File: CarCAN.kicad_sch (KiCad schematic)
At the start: 17 parts, among them IC1 TCAN337DCNR, J11 CarCANConnector, J2 CarCANConnector, U13 CDSOT23-T24CAN, U14 MCP2515-E/STVAO, Y4 8 MHz

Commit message: changed usb to be simpler (no inbuilt hub)
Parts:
- IC1: Arrow Part Number TCAN337DCNR -> (none); Arrow Price/Stock https://www.arrow.com/en/products/tcan337dcnr/texas-instrum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 -> (none); Height 1.45 -> (none); Manufacturer_Name Texas Instruments -> (none); Manufacturer_Part_Number TCAN337DCNR -> (none); Mouser Part Number 595-TCAN337DCNR -> (none); Mouser Price/Stock https://www.mouser.co.uk/ProductDetail/Texas-Instruments/TC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 -> (none)
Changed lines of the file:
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@@
-			)
-		)
-		(property "Height" "1.45"
-			(at 102.87 519.38 0)
-			(effects
-				(font
-					(size 1.27 1.27)
-				)
-				(justify left top)
-				(hide yes)
-			)
-		)
-		(property "Manufacturer_Name" "Texas Instruments"
-			(at 102.87 619.38 0)
-			(effects
-				(font
-					(size 1.27 1.27)
-				)
-				(justify left top)
-				(hide yes)
-			)
-		)
-		(property "Manufacturer_Part_Number" "TCAN337DCNR"
-			(at 102.87 719.38 0)
-			(effects
-				(font
-					(size 1.27 1.27)
-				)
-				(justify left top)
-				(hide yes)
-			)
-		)
-		(property "Mouser Part Number" "595-TCAN337DCNR"
-			(at 102.87 819.38 0)
-			(effects
-				(font
-					(size 1.27 1.27)
-				)
-				(justify left top)
-				(hide yes)
-			)
-		)
-		(property "Mouser Price/Stock" "https://www.mouser.co.uk/ProductDetail/Texas-Instruments/TCAN337DCNR?qs=gMfM3zrbS4r1ZrvbjcW09A%3D%3D"
-			(at 102.87 919.38 0)
-			(effects
-				(font
-					(size 1.27 1.27)
-				)
-				(justify left top)
-				(hide yes)
-			)
-		)
-		(property "Arrow Part Number" "TCAN337DCNR"
-			(at 102.87 1019.38 0)
-			(effects
-				(font
-					(size 1.27 1.27)
-				)
-				(justify left top)
-				(hide yes)
-			)
-		)
-		(property "Arrow Price/Stock" "https://www.arrow.com/en/products/tcan337dcnr/texas-instruments?region=nac"
-			(at 102.87 1119.38 0)
-			(effects
-				(font
-					(size 1.27 1.27)
-				)
-				(justify left top)
-				(hide yes)
 			)
 		)
@@
 			)
 		)
-		(property "Datasheet" "~"
+		(property "Datasheet" "https://abracon.com/Resonators/ABM3.pdf"
 			(at 99.06 58.42 0)
 			(effects
@@
 			)
 		)
-		(property "Datasheet" "~"
+		(property "Datasheet" "https://content.kemet.com/datasheets/KEM_C1002_X7R_SMD.pdf"
 			(at 55.88 137.16 0)
 			(effects

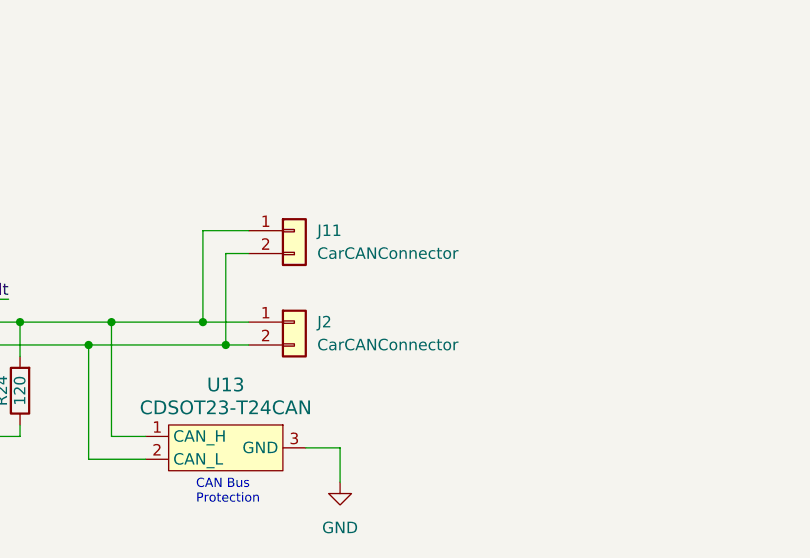
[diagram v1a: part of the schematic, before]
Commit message: moved everything to front & 0603'd stuff
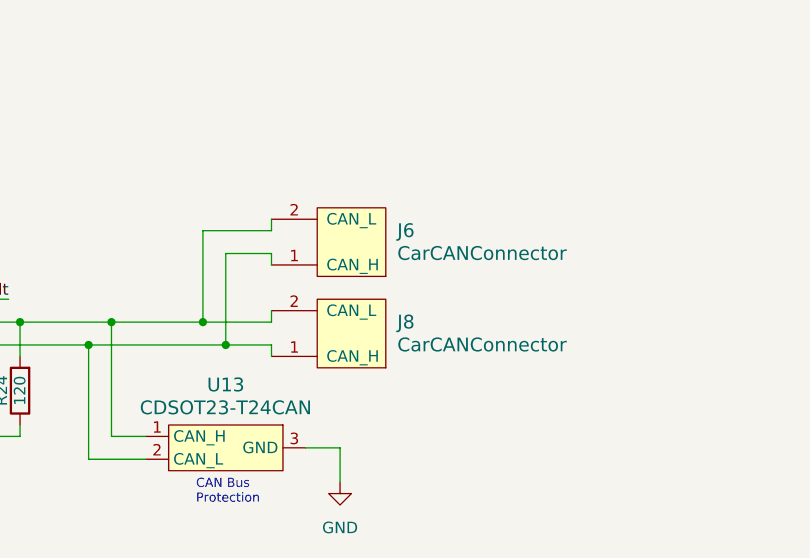
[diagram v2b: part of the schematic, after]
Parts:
- removed J11, J2: CarCANConnector, Connector_Molex:Molex_Micro-Fit_3.0_43650-0215_1x02_P3.00mm_Vertical, symbol Connector_Generic:Conn_01x02
- added J6, J8: CarCANConnector, UTSVT_Connectors:Molex_Nano-Fit_105309-xx02_1x02_P2.50mm_Vertical, symbol utsvt_connectors:CarCANConnector
- C11, C24, C25, C36, C37: footprint Capacitor_SMD:C_0805_2012Metric -> Capacitor_SMD:C_0603_1608Metric
- D4: footprint LED_SMD:LED_0805_2012Metric -> LED_SMD:LED_0603_1608Metric
- R2, R24, R34, R35: footprint Resistor_SMD:R_0805_2012Metric -> Resistor_SMD:R_0603_1608Metric
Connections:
- net at IC1.6 (CANL), R24.2, U13.1 (CAN_H): now also J6.2 (CAN_L), J8.2 (CAN_L)
- net at IC1.7 (CANH), JP1.1 (A), U13.2 (CAN_L): now also J6.1 (CAN_H), J8.1 (CAN_H)

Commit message: changed a bunch of stuff, still have work
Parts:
- C24, C25: value 22 pF -> 26 pF
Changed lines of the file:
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@@
 			)
 		)
-		(property "Value" "22 pF"
+		(property "Value" "26 pF"
 			(at 87.884 69.85 90)
 			(effects
@@
 			)
 		)
-		(property "Value" "22 pF"
+		(property "Value" "26 pF"
 			(at 87.884 59.69 90)
 			(effects

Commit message: my life is horrible
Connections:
- net CAN_L: now reaches IC1.6 (CANL), J6.2 (CAN_L), J8.2 (CAN_L), R24.2, U13.1 (CAN_H)
- net CAN_H: now reaches IC1.7 (CANH), J6.1 (CAN_H), J8.1 (CAN_H), JP1.1 (A), U13.2 (CAN_L)
- net +3.3V_PWR renamed +3.3V
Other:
- moved on the sheet: C11, C24, C25, C36, C37, D4, IC1, J6, J8, JP1, R2, R24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

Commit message: Schem done? [plz full review], redoing layout
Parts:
- R2: value 2.2k -> 700
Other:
- note added: "CAN <-> SPI"
- note added: "CAN Tranciever"
- note removed: "CAN to SPI Conversion"
- moved on the sheet: C11, C24, C25, C36, C37, D4, IC1, J6, J8, JP1, R2, R24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

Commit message: I hate my life
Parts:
- C11, C36, C37: footprint Capacitor_SMD:C_0603_1608Metric -> Capacitor_SMD:C_0603_1608Metric_Pad1.08x0.95mm_HandSolder
- C24, C25: value 26 pF -> 22 pF; footprint Capacitor_SMD:C_0603_1608Metric -> Capacitor_SMD:C_0603_1608Metric_Pad1.08x0.95mm_HandSolder
- D4: footprint LED_SMD:LED_0603_1608Metric -> LED_SMD:LED_0603_1608Metric_Pad1.05x0.95mm_HandSolder
- R2, R24, R34, R35: footprint Resistor_SMD:R_0603_1608Metric -> Resistor_SMD:R_0603_1608Metric_Pad0.98x0.95mm_HandSolder
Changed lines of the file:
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@@
 			)
 		)
-		(property "Value" "26 pF"
+		(property "Value" "22 pF"
 			(at 37.084 127 90)
 			(effects
@@
 			)
 		)
-		(property "Footprint" "Capacitor_SMD:C_0603_1608Metric"
+		(property "Footprint" "Capacitor_SMD:C_0603_1608Metric_Pad1.08x0.95mm_HandSolder"
 			(at 40.64 119.6848 0)
 			(effects
@@
 			)
 		)
-		(property "Footprint" "Capacitor_SMD:C_0603_1608Metric"
+		(property "Footprint" "Capacitor_SMD:C_0603_1608Metric_Pad1.08x0.95mm_HandSolder"
 			(at 98.7552 133.35 0)
 			(effects
@@
 			)
 		)
-		(property "Footprint" "LED_SMD:LED_0603_1608Metric"
+		(property "Footprint" "LED_SMD:LED_0603_1608Metric_Pad1.05x0.95mm_HandSolder"
 			(at 262.89 113.03 0)
 			(effects
@@
 			)
 		)
-		(property "Footprint" "Resistor_SMD:R_0603_1608Metric"
+		(property "Footprint" "Resistor_SMD:R_0603_1608Metric_Pad0.98x0.95mm_HandSolder"
 			(at 210.058 115.57 90)
 			(effects
@@
 			)
 		)
-		(property "Value" "26 pF"
+		(property "Value" "22 pF"
 			(at 37.084 116.84 90)
 			(effects
@@
 			)
 		)
-		(property "Footprint" "Capacitor_SMD:C_0603_1608Metric"
+		(property "Footprint" "Capacitor_SMD:C_0603_1608Metric_Pad1.08x0.95mm_HandSolder"
 			(at 40.64 109.5248 0)
 			(effects
@@
 			)
 		)
-		(property "Datasheet" "kicad-embed://PS-105300-100-001.pdf"
+		(property "Datasheet" "https://www.digikey.com/en/products/detail/molex/1053091102/7693146"
 			(at 229.87 106.68 0)
 			(effects
@@
 			)
 		)
-		(property "Footprint" "Resistor_SMD:R_0603_1608Metric"
+		(property "Footprint" "Resistor_SMD:R_0603_1608Metric_Pad0.98x0.95mm_HandSolder"
 			(at 191.262 99.06 90)
 			(effects
@@
 			)
 		)
-		(property "Datasheet" "kicad-embed://PS-105300-100-001.pdf"
+		(property "Datasheet" "https://www.digikey.com/en/products/detail/molex/1053091102/7693146"
 			(at 229.87 116.84 0)
 			(effects
@@
 			)
 		)
-		(property "Footprint" "Capacitor_SMD:C_0603_1608Metric"
+		(property "Footprint" "Capacitor_SMD:C_0603_1608Metric_Pad1.08x0.95mm_HandSolder"
 			(at 101.2952 91.44 0)
 			(effects
@@
 			)
 		)
-		(property "Footprint" "Resistor_SMD:R_0603_1608Metric"
+		(property "Footprint" "Resistor_SMD:R_0603_1608Metric_Pad0.98x0.95mm_HandSolder"
 			(at 261.112 104.14 90)
 			(effects
@@
 			)
 		)
-		(property "Footprint" "Resistor_SMD:R_0603_1608Metric"
+		(property "Footprint" "Resistor_SMD:R_0603_1608Metric_Pad0.98x0.95mm_HandSolder"
 			(at 92.71 126.238 90)
 			(effects
@@
 			)
 		)
-		(property "Footprint" "Capacitor_SMD:C_0603_1608Metric"
+		(property "Footprint" "Capacitor_SMD:C_0603_1608Metric_Pad1.08x0.95mm_HandSolder"
 			(at 150.8252 119.38 0)
 			(effects

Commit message: chang
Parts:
- added R5: 1000, Resistor_SMD:R_0603_1608Metric_Pad0.98x0.95mm_HandSolder, symbol Device:R
- U14: value MCP2515-E/STVAO -> MCP2515T-E/ST; P/N MCP2515-E/STVAO -> MCP2515T-E/ST
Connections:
- net +3.3V: now also R5.1; no longer C36.1, R34.2
- new net: C36.1, R34.2, R5.2
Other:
- note added: "t > 2us"
- moved on the sheet: C36, R34
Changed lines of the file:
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@@
 		)
 	)
+	(text "t > 2us"
+		(exclude_from_sim no)
+		(at 116.078 124.968 0)
+		(effects
+			(font
+				(size 1.27 1.27)
+			)
+		)
+	)
 	(text "No need to use the RX notification pins as\nthat will be also conveyed on the interrupt pin"
 		(exclude_from_sim no)
-		(at 89.916 113.792 0)
+		(at 88.138 104.902 0)
 		(effects
 			(font
@@
 	)
 	(junction
-		(at 208.28 107.95)
+		(at 106.68 124.46)
 		(diameter 0)
 		(color 0 0 0 0)
 	)
 	(junction
-		(at 193.04 105.41)
+		(at 208.28 107.95)
 		(diameter 0)
 		(color 0 0 0 0)
 	)
 	(junction
-		(at 212.09 110.49)
+		(at 193.04 105.41)
 		(diameter 0)
 		(color 0 0 0 0)
 	)
 	(junction
-		(at 30.48 115.57)
+		(at 212.09 110.49)
 		(diameter 0)
 		(color 0 0 0 0)
 	)
 	(junction
-		(at 97.79 124.46)
+		(at 30.48 115.57)
 		(diameter 0)
 		(color 0 0 0 0)
@@
 	(wire
 		(pts
-			(xy 97.79 124.46) (xy 100.33 124.46)
-		)
-		(stroke
-			(width 0)
-			(type default)
-		)
-	)
-	(wire
-		(pts
 			(xy 57.15 114.3) (xy 55.88 114.3)
 		)
@@
 	(wire
 		(pts
-			(xy 100.33 124.46) (xy 100.33 123.19)
-		)
-		(stroke
-			(width 0)
-			(type default)
-		)
-	)
-	(wire
-		(pts
 			(xy 236.22 121.92) (xy 234.95 121.92)
 		)
@@
 	(wire
 		(pts
-			(xy 96.52 124.46) (xy 97.79 124.46)
+			(xy 194.31 110.49) (xy 212.09 110.49)
 		)
 		(stroke
@@
 	(wire
 		(pts
-			(xy 194.31 110.49) (xy 212.09 110.49)
+			(xy 87.63 124.46) (xy 92.71 124.46)
 		)
 		(stroke
@@
 	(wire
 		(pts
-			(xy 87.63 124.46) (xy 88.9 124.46)
+			(xy 262.89 99.06) (xy 262.89 100.33)
 		)
 		(stroke
@@
 	(wire
 		(pts
-			(xy 262.89 99.06) (xy 262.89 100.33)
+			(xy 193.04 92.71) (xy 193.04 95.25)
 		)
 		(stroke
@@
 	(wire
 		(pts
-			(xy 193.04 92.71) (xy 193.04 95.25)
+			(xy 106.68 123.19) (xy 106.68 124.46)
 		)
 		(stroke
@@
 	(wire
 		(pts
-			(xy 97.79 133.35) (xy 97.79 134.62)
+			(xy 106.68 133.35) (xy 106.68 134.62)
 		)
 		(stroke
@@
 	(wire
 		(pts
+			(xy 106.68 114.3) (xy 106.68 115.57)
+		)
+		(stroke
+			(width 0)
+			(type default)
+		)
+	)
+	(wire
+		(pts
 			(xy 72.39 82.55) (xy 72.39 80.01)
 		)
@@
 	(wire
 		(pts
-			(xy 97.79 124.46) (xy 97.79 125.73)
+			(xy 106.68 124.46) (xy 106.68 125.73)
 		)
 		(stroke
@@
 	(wire
 		(pts
+			(xy 100.33 124.46) (xy 106.68 124.46)
+		)
+		(stroke
+			(width 0)
+			(type default)
+		)
+	)
+	(wire
+		(pts
 			(xy 26.67 115.57) (xy 30.48 115.57)
 		)
@@
 	(symbol
 		(lib_id "Device:C")
-		(at 97.79 129.54 0)
+		(at 106.68 129.54 0)
 		(unit 1)
 		(exclude_from_sim no)
@@
 		(dnp no)
 		(property "Reference" "C36"
-			(at 88.9 128.2446 0)
+			(at 109.728 128.524 0)
 			(effects
 				(font
@@
 		)
 		(property "Value" "100n"
-			(at 88.9 130.556 0)
+			(at 109.728 130.8354 0)
 			(effects
 				(font
@@
 		)
 		(property "Footprint" "Capacitor_SMD:C_0603_1608Metric_Pad1.08x0.95mm_HandSolder"
-			(at 98.7552 133.35 0)
+			(at 107.6452 133.35 0)
 			(effects
 				(font
@@
 		)
 		(property "Datasheet" "~"
-			(at 97.79 129.54 0)
+			(at 106.68 129.54 0)
 			(effects
 				(font
@@
 		)
 		(property "Description" "Unpolarized capacitor"
-			(at 97.79 129.54 0)
+			(at 106.68 129.54 0)
 			(effects
 				(font
@@
 		)
 		(property "P/N" "C0805C104M5RACTU"
-			(at 97.79 129.54 0)
+			(at 106.68 129.54 0)
 			(effects
 				(font
@@
 	(symbol
 		(lib_id "Device:R")
+		(at 106.68 119.38 0)
+		(unit 1)
+		(exclude_from_sim no)
+		(in_bom yes)
+		(on_board yes)
+		(dnp no)
+		(property "Reference" "R5"
+			(at 108.458 118.2116 0)
+			(effects
+				(font
+					(size 1.27 1.27)
+				)
+				(justify left)
+			)
+		)
+		(property "Value" "1000"
+			(at 108.458 120.523 0)
+			(effects
+				(font
+					(size 1.27 1.27)
+				)
+				(justify left)
+			)
+		)
+		(property "Footprint" "Resistor_SMD:R_0603_1608Metric_Pad0.98x0.95mm_HandSolder"
+			(at 104.902 119.38 90)
+			(effects
+				(font
+					(size 1.27 1.27)
+				)
+				(hide yes)
+			)
+		)
+		(property "Datasheet" "~"
+			(at 106.68 119.38 0)
+			(effects
+				(font
+					(size 1.27 1.27)
+				)
+				(hide yes)
+			)
+		)
+		(property "Description" "Resistor"
+			(at 106.68 119.38 0)
+			(effects
+				(font
+					(size 1.27 1.27)
+				)
+				(hide yes)
+			)
+		)
+		(property "P/N" "SDR10EZPF2200"
+			(at 106.68 119.38 0)
+			(effects
+				(font
+					(size 1.27 1.27)
+				)
+				(hide yes)
+			)
+		)
+		(pin "1"
+		)
+		(pin "2"
+		)
+		(instances
+			(project "PiBoard"
+				(path "/e4d65698-b8ec-4bf6-9f2b-a5010377155a/bb44eb34-b37d-4f19-ab49-17b4958492c8"
+					(reference "R5")
+					(unit 1)
+				)
+			)
+		)
+	)
+	(symbol
+		(lib_id "Device:R")
 		(at 193.04 99.06 0)
 		(unit 1)
@@
 	(symbol
 		(lib_id "power:GND")
-		(at 97.79 134.62 0)
+		(at 106.68 134.62 0)
 		(unit 1)
 		(exclude_from_sim no)
@@
 		(fields_autoplaced yes)
 		(property "Reference" "#PWR058"
-			(at 97.79 140.97 0)
+			(at 106.68 140.97 0)
 			(effects
 				(font
@@
 		)
 		(property "Value" "GND"
-			(at 97.79 139.7 0)
+			(at 106.68 139.7 0)
 			(effects
 				(font
@@
 		)
 		(property "Footprint" ""
-			(at 97.79 134.62 0)
+			(at 106.68 134.62 0)
 			(effects
 				(font
@@
 		)
 		(property "Datasheet" ""
-			(at 97.79 134.62 0)
+			(at 106.68 134.62 0)
 			(effects
 				(font
@@
 		)
 		(property "Description" "Power symbol creates a global label with name \"GND\" , ground"
-			(at 97.79 134.62 0)
+			(at 106.68 134.62 0)
 			(effects
 				(font
@@
 	(symbol
 		(lib_id "power:+3.3V")
-		(at 100.33 123.19 0)
+		(at 106.68 114.3 0)
 		(unit 1)
 		(exclude_from_sim no)
@@
 		(dnp no)
 		(property "Reference" "#PWR079"
-			(at 100.33 127 0)
+			(at 106.68 118.11 0)
 			(effects
 				(font
@@
 		)
 		(property "Value" "+3.3V"
-			(at 96.774 118.618 0)
+			(at 103.124 109.728 0)
 			(effects
 				(font
@@
 		)
 		(property "Footprint" ""
-			(at 100.33 123.19 0)
+			(at 106.68 114.3 0)
 			(effects
 				(font
@@
 		)
 		(property "Datasheet" ""
-			(at 100.33 123.19 0)
+			(at 106.68 114.3 0)
 			(effects
 				(font
@@
 		)
 		(property "Description" "Power symbol creates a global label with name \"+3.3V\""
-			(at 100.33 123.19 0)
+			(at 106.68 114.3 0)
 			(effects
 				(font
@@
 			)
 		)
-		(property "Value" "MCP2515-E/STVAO"
-			(at 74.5841 88.9 0)
+		(property "Value" "MCP2515T-E/ST"
+			(at 74.5333 88.9 0)
 			(effects
 				(font
@@
 			)
 		)
-		(property "Datasheet" "http://ww1.microchip.com/downloads/en/DeviceDoc/21801e.pdf"
+		(property "Datasheet" "https://ww1.microchip.com/downloads/en/DeviceDoc/MCP2515-Stand-Alone-CAN-Controller-with-SPI-20001801J.pdf"
 			(at 74.93 129.54 0)
 			(effects
@@
 			)
 		)
-		(property "P/N" "MCP2515-E/STVAO"
+		(property "P/N" "MCP2515T-E/ST"
 			(at 72.39 109.22 0)
 			(effects
@@
 	(symbol
 		(lib_id "Device:R")
-		(at 92.71 124.46 90)
+		(at 96.52 124.46 90)
 		(unit 1)
 		(exclude_from_sim no)
@@
 		(fields_autoplaced yes)
 		(property "Reference" "R34"
-			(at 92.71 118.11 90)
+			(at 96.52 118.11 90)
 			(effects
 				(font
@@
 		)
 		(property "Value" "10k"
-			(at 92.71 120.65 90)
+			(at 96.52 120.65 90)
 			(effects
 				(font
@@
 		)
 		(property "Footprint" "Resistor_SMD:R_0603_1608Metric_Pad0.98x0.95mm_HandSolder"
-			(at 92.71 126.238 90)
+			(at 96.52 126.238 90)
 			(effects
 				(font
@@
 		)
 		(property "Datasheet" "~"
-			(at 92.71 124.46 0)
+			(at 96.52 124.46 0)
 			(effects
 				(font
@@
 		)
 		(property "Description" "Resistor"
-			(at 92.71 124.46 0)
+			(at 96.52 124.46 0)
 			(effects
 				(font
@@
 		)
 		(property "P/N" "CRCW080510K0FKEAC"
-			(at 92.71 124.46 0)
+			(at 96.52 124.46 0)
 			(effects
 				(font
